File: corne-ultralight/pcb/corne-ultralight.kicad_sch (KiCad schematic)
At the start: 102 parts, among them J2 OLED, J7 OLED, SW1 SW_PUSH, SW10 SW_PUSH, SW11 SW_PUSH, SW12 SW_PUSH, SW13 SW_PUSH, SW14 SW_PUSH, SW15 SW_PUSH, SW16 SW_PUSH, SW17 SW_PUSH, SW18 SW_PUSH, SW19 SW_PUSH, SW2 SW_PUSH, SW20 SW_PUSH, SW21 SW_PUSH, SW22 SW_PUSH, SW23 SW_PUSH, SW24 SW_PUSH, SW25 SW_PUSH, SW26 SW_PUSH, SW27 SW_PUSH, SW28 SW_PUSH, SW29 SW_PUSH, SW3 SW_PUSH, SW30 SW_PUSH, SW31 SW_PUSH, SW32 SW_PUSH, SW33 SW_PUSH, SW34 SW_PUSH, SW35 SW_PUSH, SW36 SW_PUSH, SW37 SW_PUSH, SW38 SW_PUSH, SW39 SW_PUSH, SW4 SW_PUSH, SW40 SW_PUSH, SW41 SW_PUSH, SW42 SW_PUSH, SW5 SW_PUSH, SW6 SW_PUSH, SW7 SW_PUSH, SW8 SW_PUSH, SW9 SW_PUSH, U1 ProMicro, U2 ProMicro

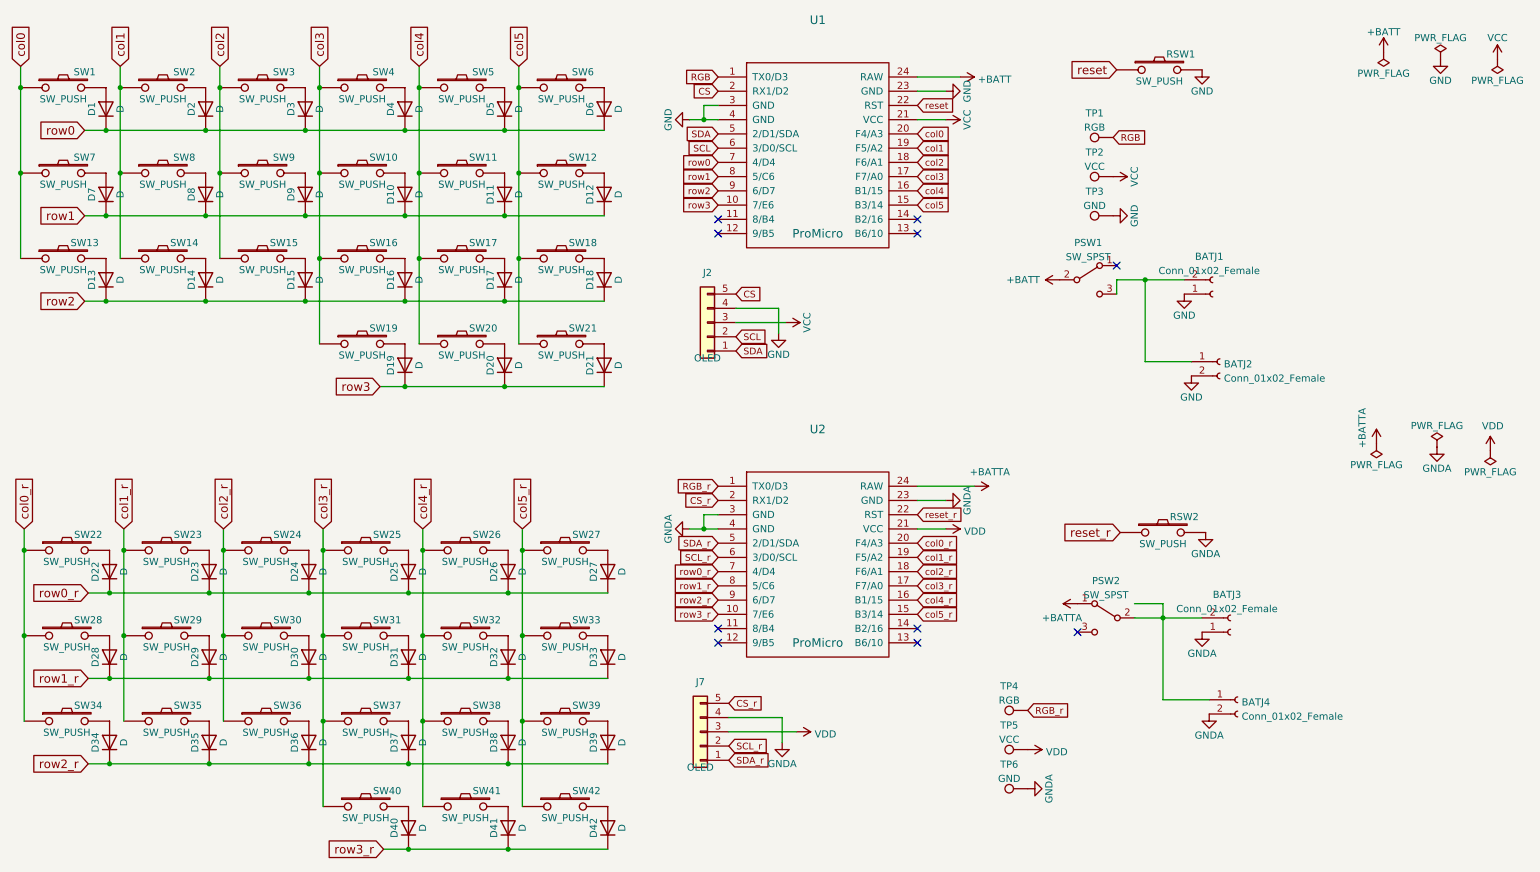
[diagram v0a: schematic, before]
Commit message: Additional JST connectors and OLED in schematics
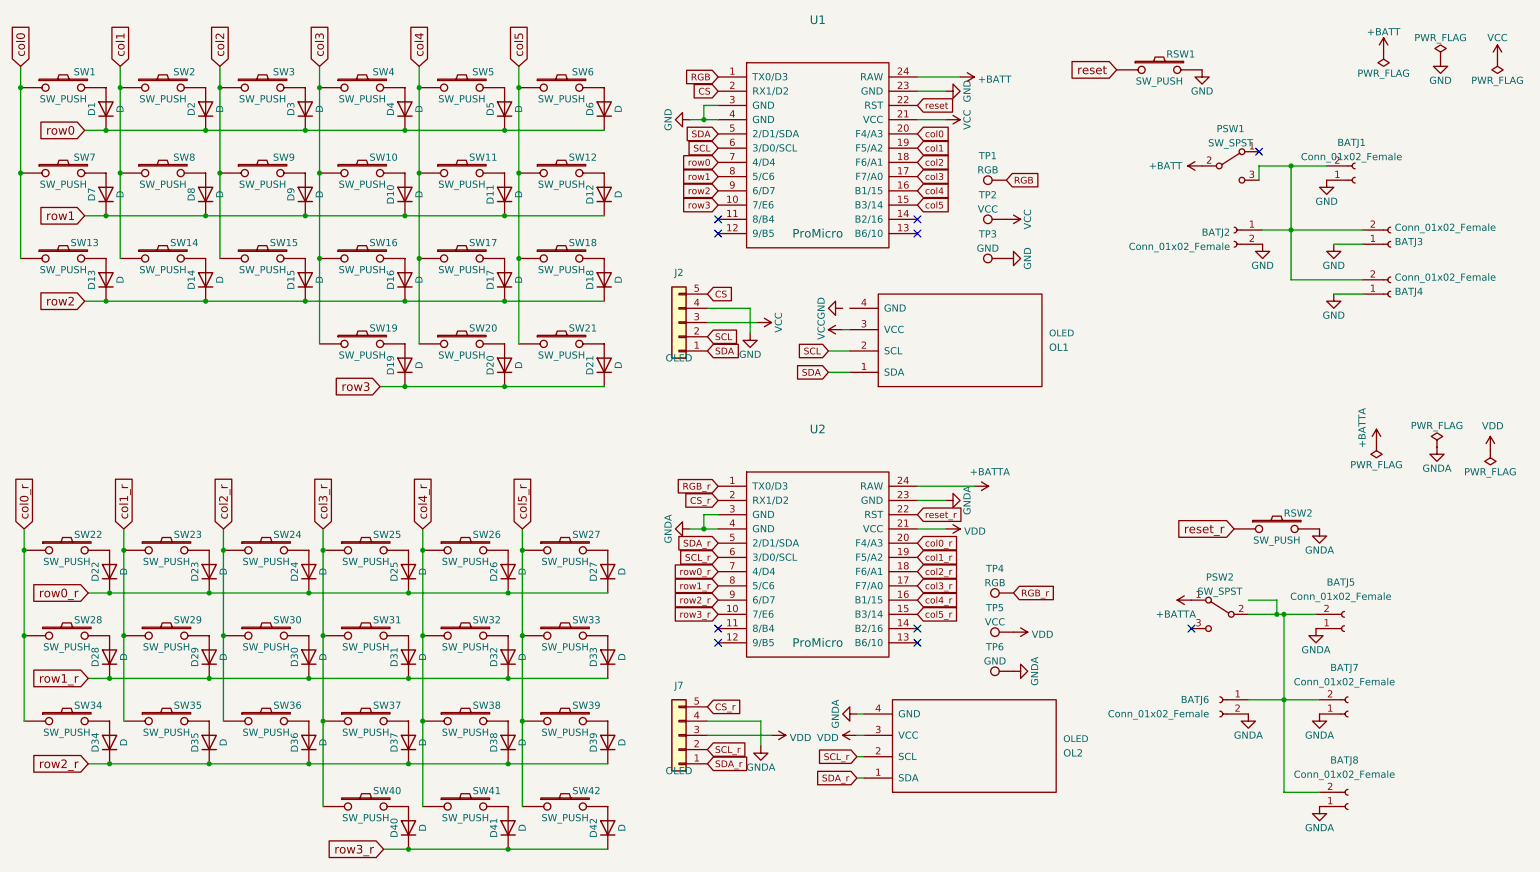
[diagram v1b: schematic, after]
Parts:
- added BATJ3, BATJ4, BATJ7, BATJ8: Conn_01x02_Female, Connector_JST:JST_PH_S2B-PH-K_1x02_P2.00mm_Horizontal, symbol Connector:Conn_01x02_Female
- added OL1, OL2: OLED, kbd:OLED_1side, symbol kbd:OLED
- BATJ1: footprint Connector_PinHeader_2.54mm:PinHeader_1x02_P2.54mm_Vertical -> Connector_JST:JST_PH_S2B-PH-K_1x02_P2.00mm_Horizontal
- BATJ5: renamed from BATJ3; footprint Connector_PinHeader_2.54mm:PinHeader_1x02_P2.54mm_Vertical -> Connector_JST:JST_PH_S2B-PH-K_1x02_P2.00mm_Horizontal
- renumbered BATJ4 to BATJ6
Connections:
- net GND: now also BATJ3.1 (Pin_1), BATJ4.1 (Pin_1)
- net GNDA: now also BATJ7.1 (Pin_1), BATJ8.1 (Pin_1), OL2.4 (GND)
- net SCL: now also OL1.2 (SCL)
- net SCL_r: now also OL2.2 (SCL)
- net SDA: now also OL1.1 (SDA)
- net SDA_r: now also OL2.1 (SDA)
- net VCC: now also OL1.3 (VCC)
- net VDD: now also OL2.3 (VCC)
- net at BATJ5.2 (Pin_2), BATJ6.1 (Pin_1), PSW2.2 (B): now also BATJ7.2 (Pin_2), BATJ8.2 (Pin_2)
- net at BATJ1.2 (Pin_2), BATJ2.1 (Pin_1), PSW1.3 (C): now also BATJ3.2 (Pin_2), BATJ4.2 (Pin_2)
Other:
- moved on the sheet: BATJ1, BATJ2, BATJ5, BATJ6, J2, J7, PSW1, PSW2, RSW2, TP1, TP2, TP3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

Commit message: Sockets fixed
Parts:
- SW1, SW10, SW11, SW12, SW13, SW14, SW15, SW16, SW17, SW18, SW19, SW2, SW20, SW3, SW4, SW5, SW6, SW7, SW8, SW9: footprint gateron-ks27:gateron-ks27-choc-v1 -> gateron-ks27:gateron-ks27-choc-v1-mx
- SW21, SW42: footprint gateron-ks27:gateron-ks27-choc-v1-1.5u -> gateron-ks27:gateron-ks27-choc-v1-mx-1.5u
- SW22, SW23, SW24, SW25, SW26, SW27, SW28, SW29, SW30, SW31, SW32, SW33, SW34, SW35, SW36, SW37, SW38, SW39, SW40, SW41: footprint gateron-ks27:gateron-ks27-choc-v1 -> gateron-ks27:gateron-ks27-choc-v1-1.5u
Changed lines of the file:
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@@
 			)
 		)
-		(property "Footprint" "gateron-ks27:gateron-ks27-choc-v1"
+		(property "Footprint" "gateron-ks27:gateron-ks27-choc-v1-mx"
 			(at 41.275 24.13 0)
 			(effects
@@
 			)
 		)
-		(property "Footprint" "gateron-ks27:gateron-ks27-choc-v1"
+		(property "Footprint" "gateron-ks27:gateron-ks27-choc-v1-mx"
 			(at 59.055 24.13 0)
 			(effects
@@
 			)
 		)
-		(property "Footprint" "gateron-ks27:gateron-ks27-choc-v1"
+		(property "Footprint" "gateron-ks27:gateron-ks27-choc-v1-mx"
 			(at 76.835 24.13 0)
 			(effects
@@
 			)
 		)
-		(property "Footprint" "gateron-ks27:gateron-ks27-choc-v1"
+		(property "Footprint" "gateron-ks27:gateron-ks27-choc-v1-mx"
 			(at 94.615 24.13 0)
 			(effects
@@
 			)
 		)
-		(property "Footprint" "gateron-ks27:gateron-ks27-choc-v1"
+		(property "Footprint" "gateron-ks27:gateron-ks27-choc-v1-mx"
 			(at 112.395 24.13 0)
 			(effects
@@
 			)
 		)
-		(property "Footprint" "gateron-ks27:gateron-ks27-choc-v1"
+		(property "Footprint" "gateron-ks27:gateron-ks27-choc-v1-mx"
 			(at 23.495 24.13 0)
 			(effects
@@
 			)
 		)
-		(property "Footprint" "gateron-ks27:gateron-ks27-choc-v1"
+		(property "Footprint" "gateron-ks27:gateron-ks27-choc-v1-mx"
 			(at 41.275 39.37 0)
 			(effects
@@
 			)
 		)
-		(property "Footprint" "gateron-ks27:gateron-ks27-choc-v1"
+		(property "Footprint" "gateron-ks27:gateron-ks27-choc-v1-mx"
 			(at 59.055 39.37 0)
 			(effects
@@
 			)
 		)
-		(property "Footprint" "gateron-ks27:gateron-ks27-choc-v1"
+		(property "Footprint" "gateron-ks27:gateron-ks27-choc-v1-mx"
 			(at 76.835 39.37 0)
 			(effects
@@
 			)
 		)
-		(property "Footprint" "gateron-ks27:gateron-ks27-choc-v1"
+		(property "Footprint" "gateron-ks27:gateron-ks27-choc-v1-mx"
 			(at 94.615 39.37 0)
 			(effects
@@
 			)
 		)
-		(property "Footprint" "gateron-ks27:gateron-ks27-choc-v1"
+		(property "Footprint" "gateron-ks27:gateron-ks27-choc-v1-mx"
 			(at 112.395 39.37 0)
 			(effects
@@
 			)
 		)
-		(property "Footprint" "gateron-ks27:gateron-ks27-choc-v1"
+		(property "Footprint" "gateron-ks27:gateron-ks27-choc-v1-mx"
 			(at 23.495 39.37 0)
 			(effects
@@
 			)
 		)
-		(property "Footprint" "gateron-ks27:gateron-ks27-choc-v1"
+		(property "Footprint" "gateron-ks27:gateron-ks27-choc-v1-mx"
 			(at 41.275 54.61 0)
 			(effects
@@
 			)
 		)
-		(property "Footprint" "gateron-ks27:gateron-ks27-choc-v1"
+		(property "Footprint" "gateron-ks27:gateron-ks27-choc-v1-mx"
 			(at 59.055 54.61 0)
 			(effects
@@
 			)
 		)
-		(property "Footprint" "gateron-ks27:gateron-ks27-choc-v1"
+		(property "Footprint" "gateron-ks27:gateron-ks27-choc-v1-mx"
 			(at 76.835 54.61 0)
 			(effects
@@
 			)
 		)
-		(property "Footprint" "gateron-ks27:gateron-ks27-choc-v1"
+		(property "Footprint" "gateron-ks27:gateron-ks27-choc-v1-mx"
 			(at 94.615 54.61 0)
 			(effects
@@
 			)
 		)
-		(property "Footprint" "gateron-ks27:gateron-ks27-choc-v1"
+		(property "Footprint" "gateron-ks27:gateron-ks27-choc-v1-mx"
 			(at 112.395 54.61 0)
 			(effects
@@
 			)
 		)
-		(property "Footprint" "gateron-ks27:gateron-ks27-choc-v1"
+		(property "Footprint" "gateron-ks27:gateron-ks27-choc-v1-mx"
 			(at 23.495 54.61 0)
 			(effects
@@
 			)
 		)
-		(property "Footprint" "gateron-ks27:gateron-ks27-choc-v1"
+		(property "Footprint" "gateron-ks27:gateron-ks27-choc-v1-mx"
 			(at 94.615 69.85 0)
 			(effects
@@
 			)
 		)
-		(property "Footprint" "gateron-ks27:gateron-ks27-choc-v1-1.5u"
+		(property "Footprint" "gateron-ks27:gateron-ks27-choc-v1-mx-1.5u"
 			(at 112.395 69.85 0)
 			(effects
@@
 			)
 		)
-		(property "Footprint" "gateron-ks27:gateron-ks27-choc-v1"
+		(property "Footprint" "gateron-ks27:gateron-ks27-choc-v1-mx"
 			(at 76.835 69.85 0)
 			(effects
@@
 			)
 		)
-		(property "Footprint" "gateron-ks27:gateron-ks27-choc-v1"
+		(property "Footprint" "gateron-ks27:gateron-ks27-choc-v1-1.5u"
 			(at 41.91 106.68 0)
 			(effects
@@
 			)
 		)
-		(property "Footprint" "gateron-ks27:gateron-ks27-choc-v1"
+		(property "Footprint" "gateron-ks27:gateron-ks27-choc-v1-1.5u"
 			(at 59.69 106.68 0)
 			(effects
@@
 			)
 		)
-		(property "Footprint" "gateron-ks27:gateron-ks27-choc-v1"
+		(property "Footprint" "gateron-ks27:gateron-ks27-choc-v1-1.5u"
 			(at 77.47 106.68 0)
 			(effects
@@
 			)
 		)
-		(property "Footprint" "gateron-ks27:gateron-ks27-choc-v1"
+		(property "Footprint" "gateron-ks27:gateron-ks27-choc-v1-1.5u"
 			(at 95.25 106.68 0)
 			(effects
@@
 			)
 		)
-		(property "Footprint" "gateron-ks27:gateron-ks27-choc-v1"
+		(property "Footprint" "gateron-ks27:gateron-ks27-choc-v1-1.5u"
 			(at 113.03 106.68 0)
 			(effects
@@
 			)
 		)
-		(property "Footprint" "gateron-ks27:gateron-ks27-choc-v1"
+		(property "Footprint" "gateron-ks27:gateron-ks27-choc-v1-1.5u"
 			(at 24.13 106.68 0)
 			(effects
@@
 			)
 		)
-		(property "Footprint" "gateron-ks27:gateron-ks27-choc-v1"
+		(property "Footprint" "gateron-ks27:gateron-ks27-choc-v1-1.5u"
 			(at 41.91 121.92 0)
 			(effects
@@
 			)
 		)
-		(property "Footprint" "gateron-ks27:gateron-ks27-choc-v1"
+		(property "Footprint" "gateron-ks27:gateron-ks27-choc-v1-1.5u"
 			(at 59.69 121.92 0)
 			(effects
@@
 			)
 		)
-		(property "Footprint" "gateron-ks27:gateron-ks27-choc-v1"
+		(property "Footprint" "gateron-ks27:gateron-ks27-choc-v1-1.5u"
 			(at 77.47 121.92 0)
 			(effects
@@
 			)
 		)
-		(property "Footprint" "gateron-ks27:gateron-ks27-choc-v1"
+		(property "Footprint" "gateron-ks27:gateron-ks27-choc-v1-1.5u"
 			(at 95.25 121.92 0)
 			(effects
@@
 			)
 		)
-		(property "Footprint" "gateron-ks27:gateron-ks27-choc-v1"
+		(property "Footprint" "gateron-ks27:gateron-ks27-choc-v1-1.5u"
 			(at 113.03 121.92 0)
 			(effects
@@
 			)
 		)
-		(property "Footprint" "gateron-ks27:gateron-ks27-choc-v1"
+		(property "Footprint" "gateron-ks27:gateron-ks27-choc-v1-1.5u"
 			(at 24.13 121.92 0)
 			(effects
@@
 			)
 		)
-		(property "Footprint" "gateron-ks27:gateron-ks27-choc-v1"
+		(property "Footprint" "gateron-ks27:gateron-ks27-choc-v1-1.5u"
 			(at 41.91 137.16 0)
 			(effects
@@
 			)
 		)
-		(property "Footprint" "gateron-ks27:gateron-ks27-choc-v1"
+		(property "Footprint" "gateron-ks27:gateron-ks27-choc-v1-1.5u"
 			(at 59.69 137.16 0)
 			(effects
@@
 			)
 		)
-		(property "Footprint" "gateron-ks27:gateron-ks27-choc-v1"
+		(property "Footprint" "gateron-ks27:gateron-ks27-choc-v1-1.5u"
 			(at 77.47 137.16 0)
 			(effects
@@
 			)
 		)
-		(property "Footprint" "gateron-ks27:gateron-ks27-choc-v1"
+		(property "Footprint" "gateron-ks27:gateron-ks27-choc-v1-1.5u"
 			(at 95.25 137.16 0)
 			(effects
@@
 			)
 		)
-		(property "Footprint" "gateron-ks27:gateron-ks27-choc-v1"
+		(property "Footprint" "gateron-ks27:gateron-ks27-choc-v1-1.5u"
 			(at 113.03 137.16 0)
 			(effects
@@
 			)
 		)
-		(property "Footprint" "gateron-ks27:gateron-ks27-choc-v1"
+		(property "Footprint" "gateron-ks27:gateron-ks27-choc-v1-1.5u"
 			(at 24.13 137.16 0)
 			(effects
@@
 			)
 		)
-		(property "Footprint" "gateron-ks27:gateron-ks27-choc-v1"
+		(property "Footprint" "gateron-ks27:gateron-ks27-choc-v1-1.5u"
 			(at 95.25 152.4 0)
 			(effects
@@
 			)
 		)
-		(property "Footprint" "gateron-ks27:gateron-ks27-choc-v1-1.5u"
+		(property "Footprint" "gateron-ks27:gateron-ks27-choc-v1-mx-1.5u"
 			(at 113.03 152.4 0)
 			(effects
@@
 			)
 		)
-		(property "Footprint" "gateron-ks27:gateron-ks27-choc-v1"
+		(property "Footprint" "gateron-ks27:gateron-ks27-choc-v1-1.5u"
 			(at 77.47 152.4 0)
 			(effects

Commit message: PCB updated with additional components
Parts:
- SW22, SW23, SW24, SW25, SW26, SW27, SW28, SW29, SW30, SW31, SW32, SW33, SW34, SW35, SW36, SW37, SW38, SW39, SW40, SW41: footprint gateron-ks27:gateron-ks27-choc-v1-1.5u -> gateron-ks27:gateron-ks27-choc-v1-mx
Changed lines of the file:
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@@
 			)
 		)
-		(property "Footprint" "gateron-ks27:gateron-ks27-choc-v1-1.5u"
+		(property "Footprint" "gateron-ks27:gateron-ks27-choc-v1-mx"
 			(at 41.91 106.68 0)
 			(effects
@@
 			)
 		)
-		(property "Footprint" "gateron-ks27:gateron-ks27-choc-v1-1.5u"
+		(property "Footprint" "gateron-ks27:gateron-ks27-choc-v1-mx"
 			(at 59.69 106.68 0)
 			(effects
@@
 			)
 		)
-		(property "Footprint" "gateron-ks27:gateron-ks27-choc-v1-1.5u"
+		(property "Footprint" "gateron-ks27:gateron-ks27-choc-v1-mx"
 			(at 77.47 106.68 0)
 			(effects
@@
 			)
 		)
-		(property "Footprint" "gateron-ks27:gateron-ks27-choc-v1-1.5u"
+		(property "Footprint" "gateron-ks27:gateron-ks27-choc-v1-mx"
 			(at 95.25 106.68 0)
 			(effects
@@
 			)
 		)
-		(property "Footprint" "gateron-ks27:gateron-ks27-choc-v1-1.5u"
+		(property "Footprint" "gateron-ks27:gateron-ks27-choc-v1-mx"
 			(at 113.03 106.68 0)
 			(effects
@@
 			)
 		)
-		(property "Footprint" "gateron-ks27:gateron-ks27-choc-v1-1.5u"
+		(property "Footprint" "gateron-ks27:gateron-ks27-choc-v1-mx"
 			(at 24.13 106.68 0)
 			(effects
@@
 			)
 		)
-		(property "Footprint" "gateron-ks27:gateron-ks27-choc-v1-1.5u"
+		(property "Footprint" "gateron-ks27:gateron-ks27-choc-v1-mx"
 			(at 41.91 121.92 0)
 			(effects
@@
 			)
 		)
-		(property "Footprint" "gateron-ks27:gateron-ks27-choc-v1-1.5u"
+		(property "Footprint" "gateron-ks27:gateron-ks27-choc-v1-mx"
 			(at 59.69 121.92 0)
 			(effects
@@
 			)
 		)
-		(property "Footprint" "gateron-ks27:gateron-ks27-choc-v1-1.5u"
+		(property "Footprint" "gateron-ks27:gateron-ks27-choc-v1-mx"
 			(at 77.47 121.92 0)
 			(effects
@@
 			)
 		)
-		(property "Footprint" "gateron-ks27:gateron-ks27-choc-v1-1.5u"
+		(property "Footprint" "gateron-ks27:gateron-ks27-choc-v1-mx"
 			(at 95.25 121.92 0)
 			(effects
@@
 			)
 		)
-		(property "Footprint" "gateron-ks27:gateron-ks27-choc-v1-1.5u"
+		(property "Footprint" "gateron-ks27:gateron-ks27-choc-v1-mx"
 			(at 113.03 121.92 0)
 			(effects
@@
 			)
 		)
-		(property "Footprint" "gateron-ks27:gateron-ks27-choc-v1-1.5u"
+		(property "Footprint" "gateron-ks27:gateron-ks27-choc-v1-mx"
 			(at 24.13 121.92 0)
 			(effects
@@
 			)
 		)
-		(property "Footprint" "gateron-ks27:gateron-ks27-choc-v1-1.5u"
+		(property "Footprint" "gateron-ks27:gateron-ks27-choc-v1-mx"
 			(at 41.91 137.16 0)
 			(effects
@@
 			)
 		)
-		(property "Footprint" "gateron-ks27:gateron-ks27-choc-v1-1.5u"
+		(property "Footprint" "gateron-ks27:gateron-ks27-choc-v1-mx"
 			(at 59.69 137.16 0)
 			(effects
@@
 			)
 		)
-		(property "Footprint" "gateron-ks27:gateron-ks27-choc-v1-1.5u"
+		(property "Footprint" "gateron-ks27:gateron-ks27-choc-v1-mx"
 			(at 77.47 137.16 0)
 			(effects
@@
 			)
 		)
-		(property "Footprint" "gateron-ks27:gateron-ks27-choc-v1-1.5u"
+		(property "Footprint" "gateron-ks27:gateron-ks27-choc-v1-mx"
 			(at 95.25 137.16 0)
 			(effects
@@
 			)
 		)
-		(property "Footprint" "gateron-ks27:gateron-ks27-choc-v1-1.5u"
+		(property "Footprint" "gateron-ks27:gateron-ks27-choc-v1-mx"
 			(at 113.03 137.16 0)
 			(effects
@@
 			)
 		)
-		(property "Footprint" "gateron-ks27:gateron-ks27-choc-v1-1.5u"
+		(property "Footprint" "gateron-ks27:gateron-ks27-choc-v1-mx"
 			(at 24.13 137.16 0)
 			(effects
@@
 			)
 		)
-		(property "Footprint" "gateron-ks27:gateron-ks27-choc-v1-1.5u"
+		(property "Footprint" "gateron-ks27:gateron-ks27-choc-v1-mx"
 			(at 95.25 152.4 0)
 			(effects
@@
 			)
 		)
-		(property "Footprint" "gateron-ks27:gateron-ks27-choc-v1-1.5u"
+		(property "Footprint" "gateron-ks27:gateron-ks27-choc-v1-mx"
 			(at 77.47 152.4 0)
 			(effects
